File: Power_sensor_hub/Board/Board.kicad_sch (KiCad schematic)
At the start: 91 parts, among them J1 ICSP, J2 USB_B_Micro, U1 ATmega32U4-A, U2 HC-SR04, U3 to-5V, U4 to-6V, U6 to-3V3, Y1 16MHz

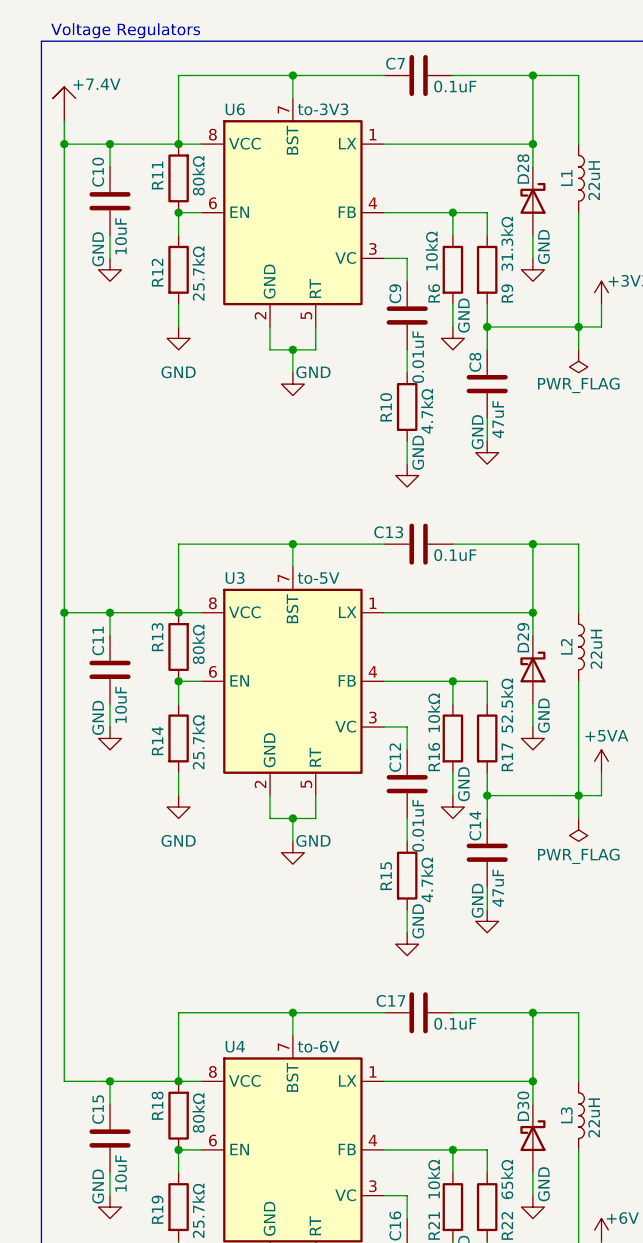
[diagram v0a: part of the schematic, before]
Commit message: created skeleton/starter code
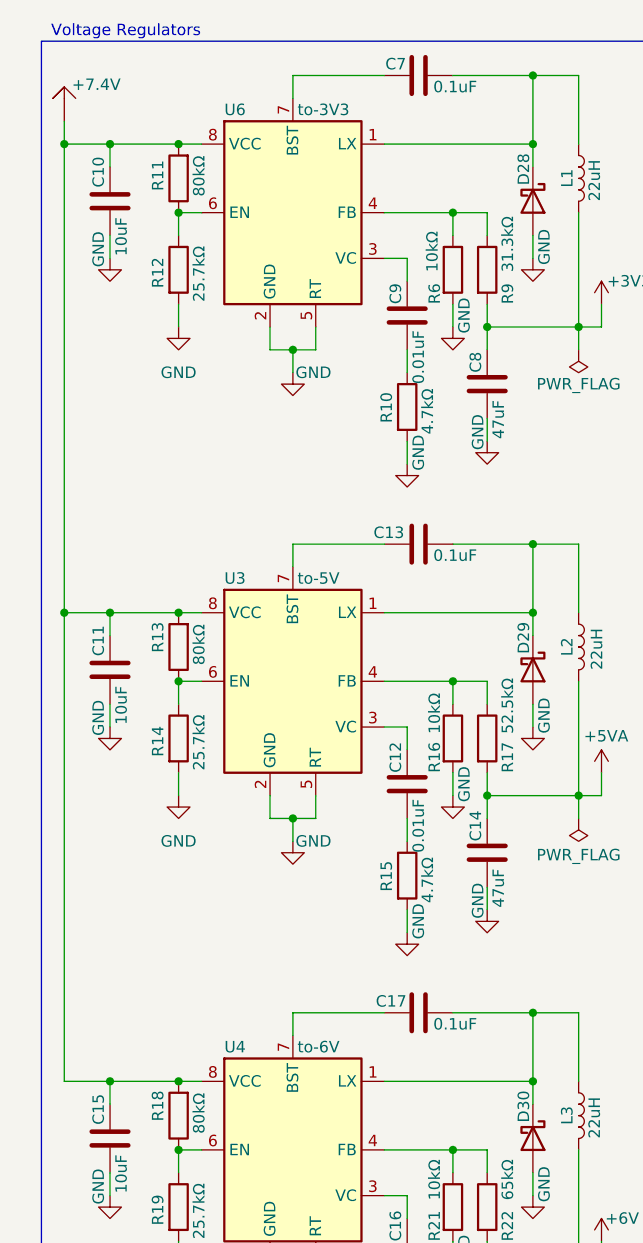
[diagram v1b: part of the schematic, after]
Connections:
- net +7.4V: no longer C13.1, C17.1, C7.1, U3.7 (BST), U4.7 (BST), U6.7 (BST)
- new net: C13.1, U3.7 (BST)
- new net: C17.1, U4.7 (BST)
- new net: C7.1, U6.7 (BST)
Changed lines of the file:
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@@
-	)
-	(junction
-		(at 41.91 20.32)
-		(diameter 0)
-		(color 0 0 0 0)
-	)
-	(junction
-		(at 41.91 72.39)
-		(diameter 0)
-		(color 0 0 0 0)
 	)
 	(junction
@@
 		(color 0 0 0 0)
 	)
-	(junction
-		(at 41.91 124.46)
-		(diameter 0)
-		(color 0 0 0 0)
-	)
 	(no_connect
 		(at 171.45 78.74)
@@
 	(wire
 		(pts
-			(xy 29.21 27.94) (xy 29.21 20.32)
-		)
-		(stroke
-			(width 0)
-			(type default)
-		)
-	)
-	(wire
-		(pts
 			(xy 147.32 138.43) (xy 149.86 138.43)
 		)
@@
 	(wire
 		(pts
-			(xy 29.21 124.46) (xy 41.91 124.46)
-		)
-		(stroke
-			(width 0)
-			(type default)
-		)
-	)
-	(wire
-		(pts
 			(xy 16.51 132.08) (xy 21.59 132.08)
 		)
@@
 	(wire
 		(pts
-			(xy 29.21 72.39) (xy 41.91 72.39)
-		)
-		(stroke
-			(width 0)
-			(type default)
-		)
-	)
-	(wire
-		(pts
 			(xy 168.91 96.52) (xy 171.45 96.52)
 		)
@@
 	(wire
 		(pts
-			(xy 29.21 20.32) (xy 41.91 20.32)
-		)
-		(stroke
-			(width 0)
-			(type default)
-		)
-	)
-	(wire
-		(pts
 			(xy 29.21 132.08) (xy 31.75 132.08)
 		)
@@
 	(wire
 		(pts
-			(xy 29.21 80.01) (xy 29.21 72.39)
-		)
-		(stroke
-			(width 0)
-			(type default)
-		)
-	)
-	(wire
-		(pts
 			(xy 168.91 50.8) (xy 171.45 50.8)
 		)
@@
 		)
 		(stroke
-			(width 0)
-			(type default)
-		)
-	)
-	(wire
-		(pts
-			(xy 29.21 132.08) (xy 29.21 124.46)
-		)
-		(stroke
